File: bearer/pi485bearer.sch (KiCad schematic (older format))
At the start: 19 parts, among them P1 PWR, P2 Rasperry Pi, P3 Latch Disable, P4 TERM, Q1 2N4401, Q2 2N4401, Q3 2N4401, U1 NE555

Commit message: Renamed bearer.
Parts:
- C1: symbol CAP -> C
- D3: symbol DIODE -> D
- R7: value R -> 120
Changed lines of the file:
@@
 LIBS:contrib
 LIBS:valves
-LIBS:pi485carrier-cache
+LIBS:pi485bearer-cache
 EELAYER 26 0
 EELAYER END
@@
 encoding utf-8
 Sheet 1 2
-Title "Pi485"
+Title "Pi485 Bearer"
 Date "2017-01-18"
 Rev "1.1.0"
 Comp "Bryan Varner"
 Comment1 ""
-Comment2 "Size resistor values R1, R3, and R7 appropriately for your LED choices."
+Comment2 "Size resistor values R3 and R4 appropriately for your LED choices."
 Comment3 "Implements half-duplex with TX latched RE/DE"
 Comment4 "Raspberry Pi / Arduino UART to RS485"
@@
 $EndComp
 $Comp
-L CAP C1
+L C C1
 U 1 1 5881B0E4
 P 6150 5450
@@
 $EndComp
 $Comp
-L DIODE D3
+L D D3
 U 1 1 5881B0FC
 P 5850 4400
@@
 P 7550 3150
 F 0 "R7" H 7620 3196 50  0000 L CNN
-F 1 "R" H 7620 3105 50  0000 L CNN
+F 1 "120" H 7620 3105 50  0000 L CNN
 F 2 "Resistors_THT:Resistor_Horizontal_RM10mm" V 7480 3150 50  0001 C CNN
 F 3 "" H 7550 3150 50  0000 C CNN
@@
 Connection ~ 6400 4850
 Wire Wire Line
-	5000 5450 5900 5450
+	5000 5450 6000 5450
 Wire Wire Line
 	5500 5250 5500 5650
@@
 	6400 3800 6400 4000
 Wire Wire Line
-	5650 4400 4850 4400
+	5700 4400 4850 4400
 Wire Wire Line
 	2900 4300 2900 4850
@@
 Connection ~ 4000 3000
 Wire Wire Line
-	6050 4400 6400 4400
+	6000 4400 6400 4400
 Connection ~ 6400 5050
 Wire Wire Line
@@
 	6650 4650 6650 3450
 Wire Wire Line
-	6650 3450 5800 3450
-Wire Wire Line
-	5800 3450 5800 2850
+	5800 3450 6650 3450
+Wire Wire Line
+	5800 2850 5800 3450
 Wire Wire Line
 	5800 3000 5900 3000
@@
 Wire Wire Line
 	5400 2000 7200 2000
+Wire Wire Line
+	6400 5450 6300 5450
 $EndSCHEMATC

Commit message: Updated with TERM / RO values in schemas and PCBs
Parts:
- P3: value Latch Disable -> RO
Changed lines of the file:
@@
 P 4800 5400
 F 0 "P3" H 4800 5550 50  0000 C CNN
-F 1 "Latch Disable" V 4900 5400 50  0000 C CNN
+F 1 "RO" V 4900 5400 50  0000 C CNN
 F 2 "Pin_Headers:Pin_Header_Straight_1x02" H 5450 5650 50  0001 C CNN
 F 3 "" H 4800 5400 50  0000 C CNN

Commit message: Low-side NPN switching. We'll see if things 'floating' causes issues... if so, I'll have to order a few PNP's to use for high-side switching.
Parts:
- Q1, Q2, Q3: symbol BC413 -> Q_NPN_EBC
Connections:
- net GND: now also Q3.1 (E); no longer C1.2, D1.1 (K), D2.1 (K), P3.1 (P1), Q1.3 (E), Q2.3 (E), U1.1 (GND)
- net VCC: now also R1.2, R2.2, R6.2, U1.4 (R), U1.8 (VCC); no longer Q3.1 (C)
- net at D1.2 (A), R1.1: now also Q1.3 (C); no longer Q1.1 (C)
- net at D2.2 (A), R2.1: now also Q2.3 (C); no longer Q2.1 (C)
- removed net lctec485/VCIN: Q3.3 (E), R1.2, R2.2, R6.2, U1.4 (R), U1.8 (VCC)
- new net lctec485/GND: C1.2, D1.1 (K), D2.1 (K), P3.1 (P1), Q1.1 (E), Q2.1 (E), Q3.3 (C), U1.1 (GND)
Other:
- moved on the sheet: C1, D1, D2, D3, P3, R1, R2, R3, R4, R5, R6, U1

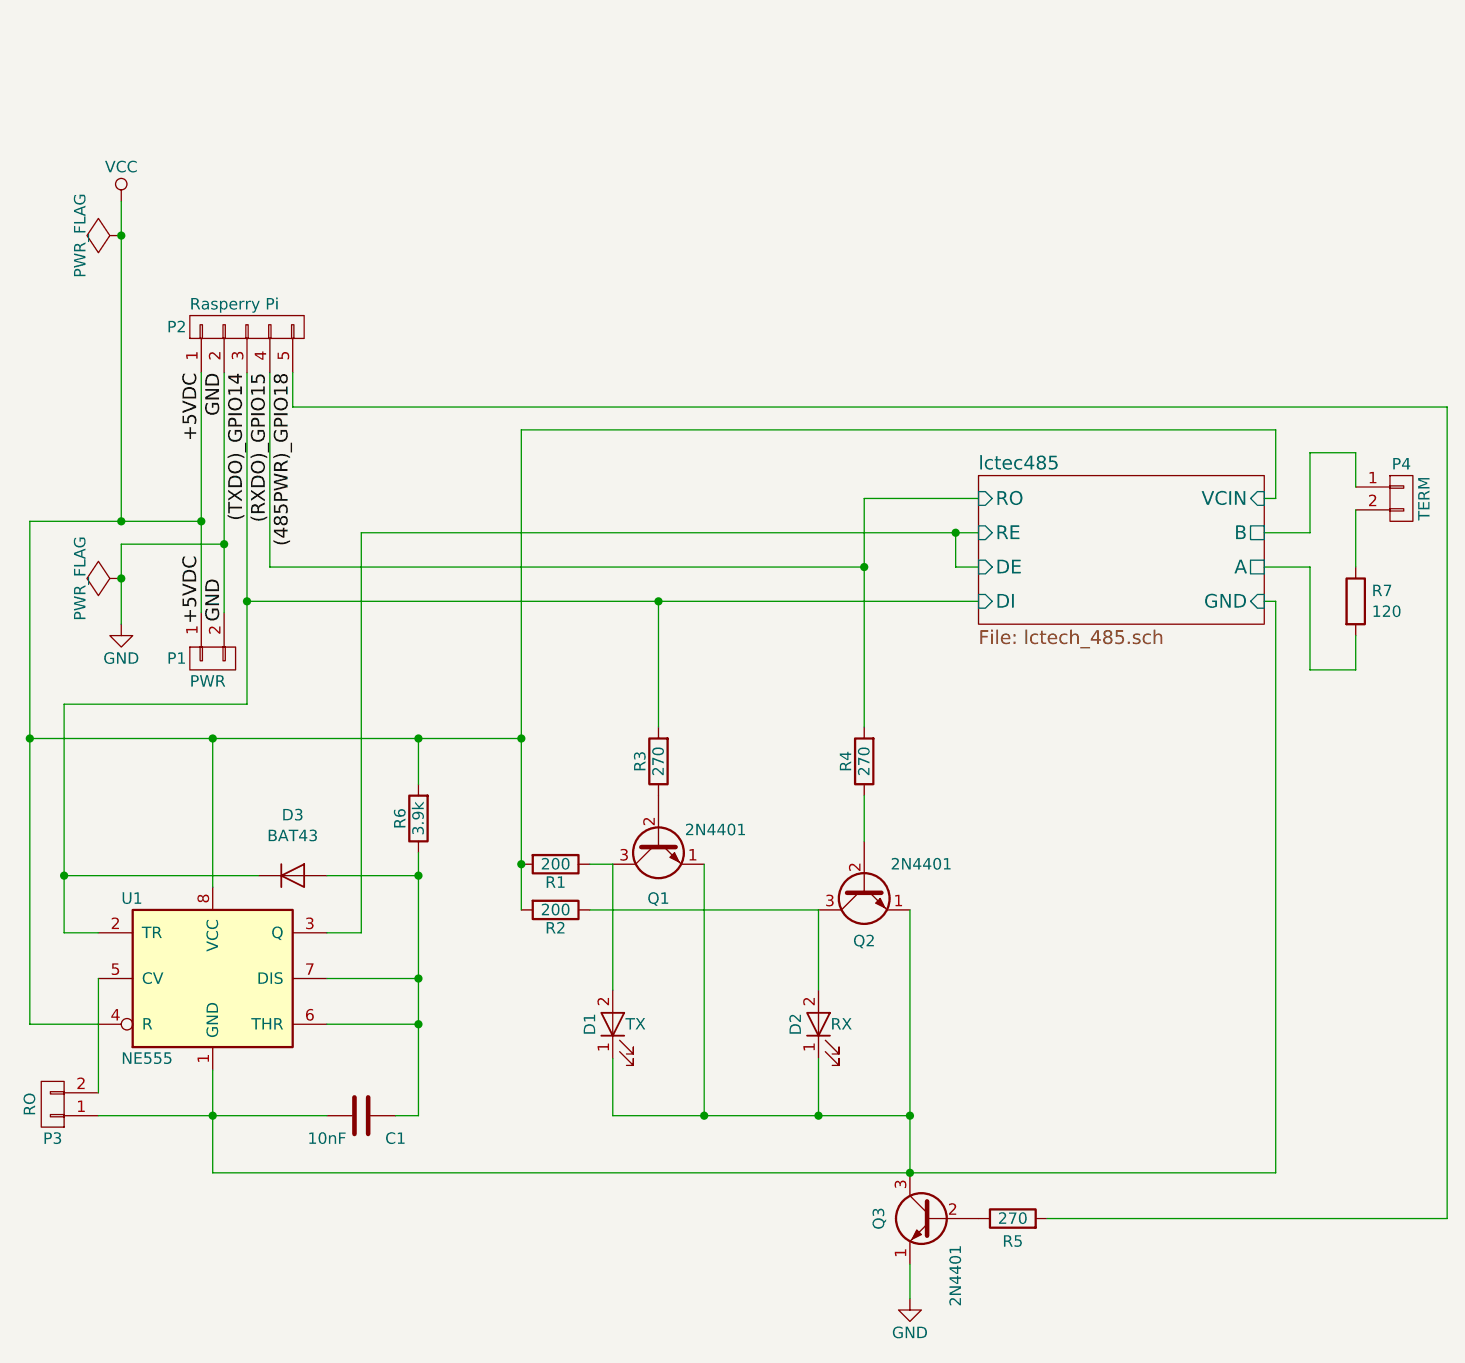
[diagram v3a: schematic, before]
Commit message: high-side PNP power switching for the bearer.
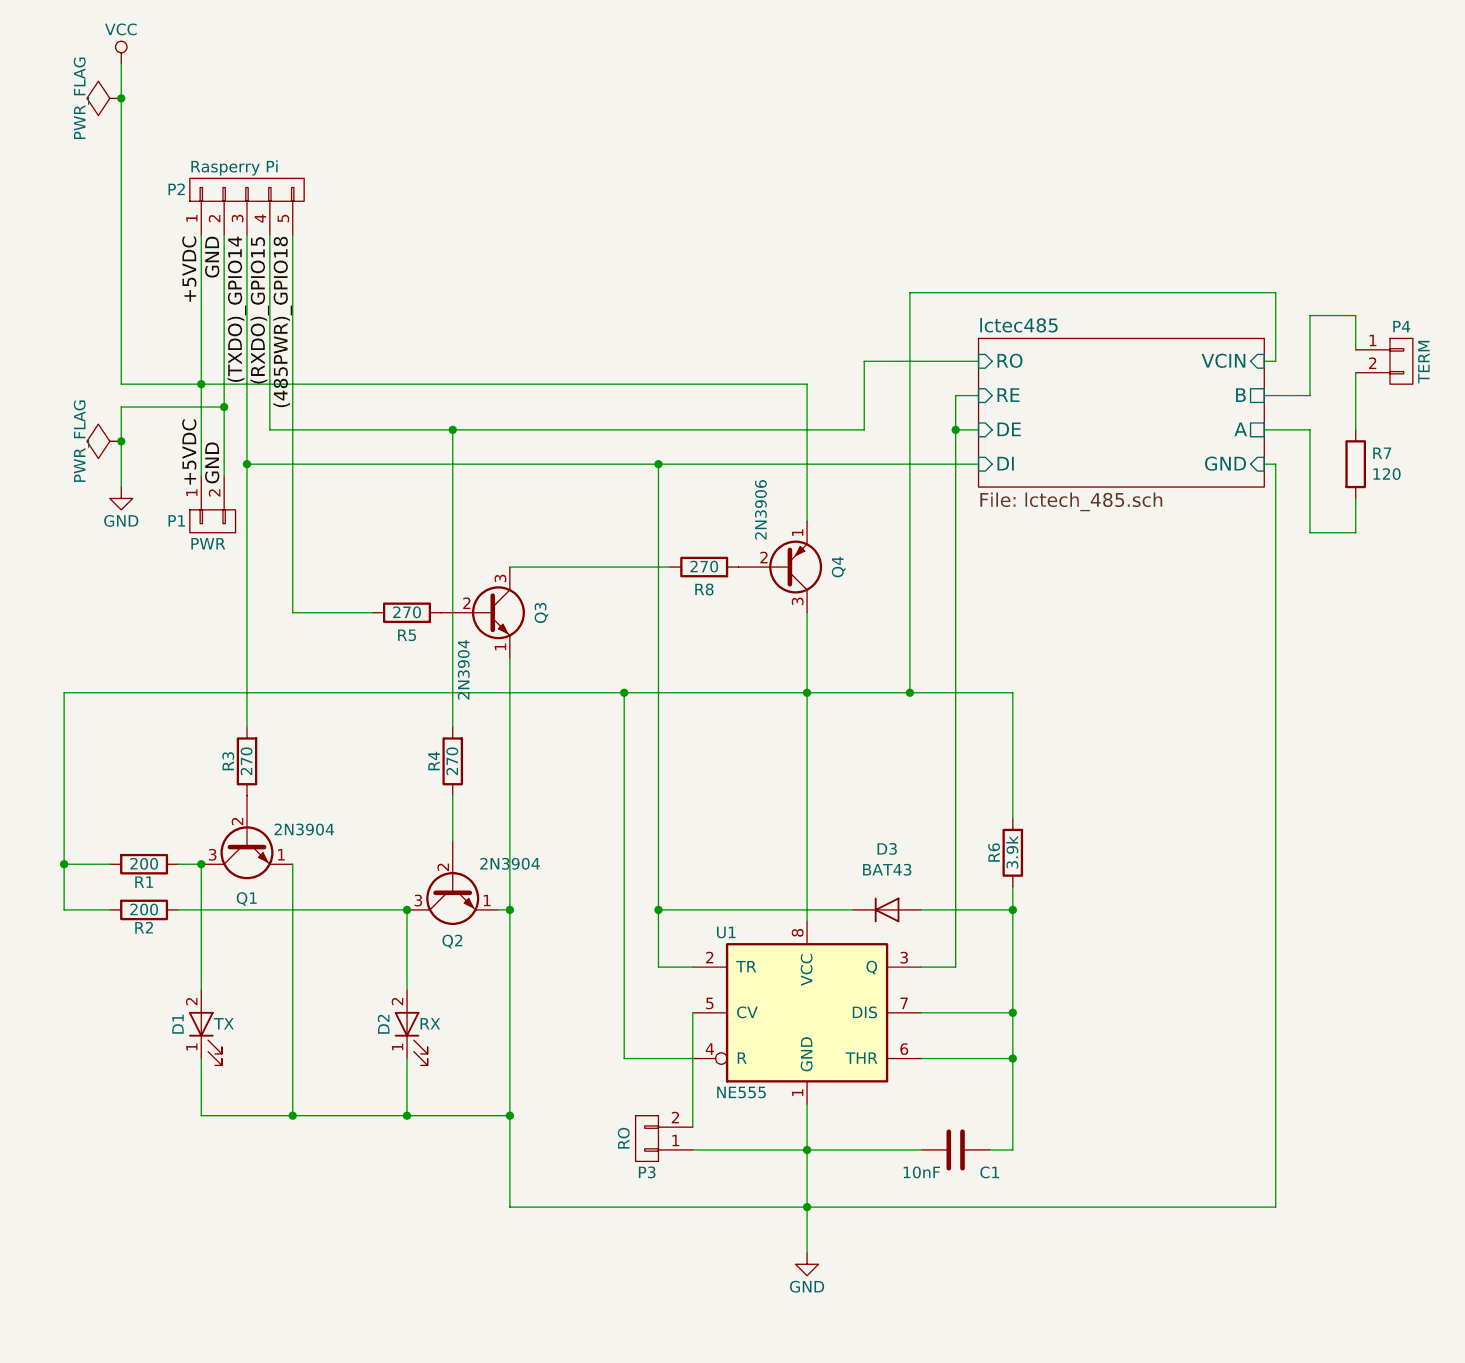
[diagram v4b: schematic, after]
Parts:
- added Q4: 2N3906, TO_SOT_Packages_THT:TO-92_Inline_Wide, symbol Q_PNP_EBC
- added R8: 270, Resistors_THT:Resistor_Horizontal_RM10mm, symbol R
- Q1, Q2, Q3: value 2N4401 -> 2N3904
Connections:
- net (485PWR)_GPIO18: now also R5.1; no longer R5.2
- net GND: now also C1.2, D1.1 (K), D2.1 (K), P3.1 (P1), Q1.1 (E), Q2.1 (E), U1.1 (GND)
- net VCC: now also Q4.1 (E); no longer R1.2, R2.2, R6.2, U1.4 (R), U1.8 (VCC)
- net at Q3.2 (B): now also R5.2; no longer R5.1
- removed net lctec485/GND: C1.2, D1.1 (K), D2.1 (K), P3.1 (P1), Q1.1 (E), Q2.1 (E), Q3.3 (C), U1.1 (GND)
- new net: Q3.3 (C), R8.1
- new net: Q4.2 (B), R8.2
- new net lctec485/VCIN: Q4.3 (C), R1.2, R2.2, R6.2, U1.4 (R), U1.8 (VCC)
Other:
- moved on the sheet: C1, D1, D2, D3, P1, P2, P3, P4, Q1, Q2, Q3, R1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

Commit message: 1.1.1 schematics, trace plots, etc.
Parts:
- added C2: 10nF, Capacitors_THT:C_Rect_L4_W2.5_P2.5, symbol C
- added R9: 4.7k, Resistors_THT:Resistor_Horizontal_RM15mm, symbol R
- C1: footprint Capacitors_THT:C_Rect_L7_W2.5_P5 -> Capacitors_THT:C_Rect_L4_W2.5_P2.5
- R1, R2, R4, R5, R8: footprint Resistors_THT:Resistor_Horizontal_RM10mm -> Resistors_THT:Resistor_Horizontal_RM7mm
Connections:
- net GND: now also P3.2 (P2), C2.1, R9.2; no longer P3.1 (P1)
- net lctec485/DE: now also R9.1
- net at U1.5 (CV): now also P3.1 (P1), C2.2; no longer P3.2 (P2)
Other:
- moved on the sheet: P3
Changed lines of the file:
@@
 Sheet 1 2
 Title "Pi485 Bearer"
-Date "2017-02-12"
-Rev "1.1.0"
+Date "2017-02-20"
+Rev "1.1.1"
 Comp "Bryan Varner"
 Comment1 ""
@@
 F 0 "C1" V 5900 5700 50  0000 C CNN
 F 1 "10nF" V 5900 5400 50  0000 C CNN
-F 2 "Capacitors_THT:C_Rect_L7_W2.5_P5" V 6000 5250 50  0001 C CNN
+F 2 "Capacitors_THT:C_Rect_L4_W2.5_P2.5" V 6000 5250 50  0001 C CNN
 F 3 "" H 5800 5550 50  0000 C CNN
 	1    5800 5550
@@
 F 0 "R2" V 2330 4500 50  0000 C CNN
 F 1 "200" V 2250 4500 50  0000 C CNN
-F 2 "Resistors_THT:Resistor_Horizontal_RM10mm" V 2400 3800 50  0001 C CNN
+F 2 "Resistors_THT:Resistor_Horizontal_RM7mm" V 2400 3800 50  0001 C CNN
 F 3 "" H 2250 4500 50  0000 C CNN
 	1    2250 4500
@@
 F 0 "R1" V 2330 4300 50  0000 C CNN
 F 1 "200" V 2250 4300 50  0000 C CNN
-F 2 "Resistors_THT:Resistor_Horizontal_RM10mm" V 2400 3600 50  0001 C CNN
+F 2 "Resistors_THT:Resistor_Horizontal_RM7mm" V 2400 3600 50  0001 C CNN
 F 3 "" H 2250 4300 50  0000 C CNN
 	1    2250 4300
@@
 F 0 "R4" V 3680 3850 50  0000 C CNN
 F 1 "270" V 3600 3850 50  0000 C CNN
-F 2 "Resistors_THT:Resistor_Horizontal_RM10mm" V 3750 3150 50  0001 C CNN
+F 2 "Resistors_THT:Resistor_Horizontal_RM7mm" V 3750 3150 50  0001 C CNN
 F 3 "" H 3600 3850 50  0000 C CNN
 	1    3600 3850
@@
 $EndComp
 $Comp
-L CONN_01X02 P3
-U 1 1 5881B0FD
-P 4450 5500
-F 0 "P3" H 4450 5650 50  0000 C CNN
-F 1 "RO" V 4550 5500 50  0000 C CNN
-F 2 "Pin_Headers:Pin_Header_Straight_1x02" H 5100 5750 50  0001 C CNN
-F 3 "" H 4450 5500 50  0000 C CNN
-	1    4450 5500
-	-1   0    0    1
-$EndComp
-$Comp
 L R R5
 U 1 1 5881B0FE
@@
 F 0 "R5" V 3300 3200 50  0000 C CNN
 F 1 "270" V 3400 3200 50  0000 C CNN
-F 2 "Resistors_THT:Resistor_Horizontal_RM10mm" V 3550 2500 50  0001 C CNN
+F 2 "Resistors_THT:Resistor_Horizontal_RM7mm" V 3550 2500 50  0001 C CNN
 F 3 "" H 3400 3200 50  0000 C CNN
 	1    3400 3200
@@
 Connection ~ 6050 4950
 Wire Wire Line
-	4650 5550 5650 5550
+	4400 5500 4550 5500
+Wire Wire Line
+	4550 5550 5650 5550
 Wire Wire Line
 	5150 5350 5150 6000
@@
 Connection ~ 6050 5150
 Wire Wire Line
-	4650 5450 4650 4950
+	4150 4950 4650 4950
 Wire Wire Line
 	2500 5400 3850 5400
@@
 	7150 2550 7200 2550
 Wire Wire Line
-	7200 5800 7200 2550
+	7200 2550 7200 5800
 Wire Wire Line
 	5400 2100 5900 2100
@@
 	5800 2250 5800 4750
 Wire Wire Line
-	5800 4750 5650 4750
-Wire Wire Line
-	3850 5800 7200 5800
+	5650 4750 6300 4750
+Wire Wire Line
+	7200 5800 3850 5800
 Wire Wire Line
 	7200 1800 7200 2100
@@
 F 0 "R8" V 4600 3000 50  0000 C CNN
 F 1 "270" V 4700 3000 50  0000 C CNN
-F 2 "Resistors_THT:Resistor_Horizontal_RM10mm" V 4850 2300 50  0001 C CNN
+F 2 "Resistors_THT:Resistor_Horizontal_RM7mm" V 4850 2300 50  0001 C CNN
 F 3 "" H 4700 3000 50  0000 C CNN
 	1    4700 3000
@@
 Connection ~ 4350 3550
 Connection ~ 4500 2550
+$Comp
+L R R9
+U 1 1 58A868D1
+P 6300 5000
+F 0 "R9" V 6380 5000 50  0000 C CNN
+F 1 "4.7k" V 6300 5000 50  0000 C CNN
+F 2 "Resistors_THT:Resistor_Horizontal_RM15mm" H 5400 5000 50  0001 C CNN
+F 3 "" H 6300 5000 50  0000 C CNN
+	1    6300 5000
+	1    0    0    -1
+$EndComp
+Connection ~ 5800 4750
+Wire Wire Line
+	6300 5150 6300 5800
+Connection ~ 6300 5800
+$Comp
+L C C2
+U 1 1 58A86CE6
+P 4350 5650
+F 0 "C2" V 4450 5800 50  0000 C CNN
+F 1 "10nF" V 4450 5500 50  0000 C CNN
+F 2 "Capacitors_THT:C_Rect_L4_W2.5_P2.5" V 4550 5350 50  0001 C CNN
+F 3 "" H 4350 5650 50  0000 C CNN
+	1    4350 5650
+	0    1    1    0
+$EndComp
+Wire Wire Line
+	4150 4950 4150 5650
+Wire Wire Line
+	6300 4750 6300 4850
+Wire Wire Line
+	4150 5650 4200 5650
+Wire Wire Line
+	4500 5650 4550 5650
+Wire Wire Line
+	4550 5650 4550 5500
+Connection ~ 4550 5550
+$Comp
+L CONN_01X02 P3
+U 1 1 5881B0FD
+P 4350 5300
+F 0 "P3" H 4350 5450 50  0000 C CNN
+F 1 "RO" V 4450 5300 50  0000 C CNN
+F 2 "Pin_Headers:Pin_Header_Straight_1x02" H 5000 5550 50  0001 C CNN
+F 3 "" H 4350 5300 50  0000 C CNN
+	1    4350 5300
+	0    -1   -1   0
+$EndComp
+Wire Wire Line
+	4300 5500 4150 5500
+Connection ~ 4150 5500
 $EndSCHEMATC

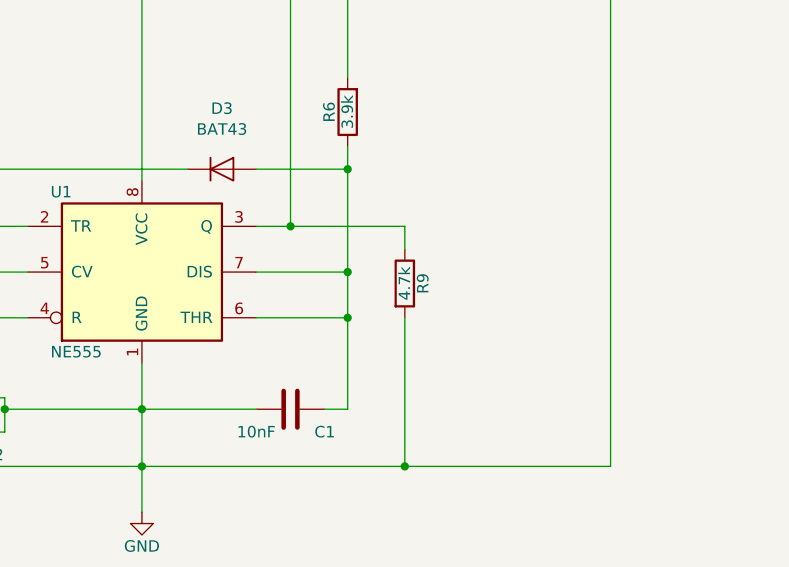
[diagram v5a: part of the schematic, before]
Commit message: Updates for jumpered biasing on standalone boards. The silly bearer modules you can just unsolder the biasing resistors if it becomes an issue. I should probably add jumpering for that too, but at this point, I just don't much care. A slight modification to those silly SMT boards really isn't that hard...
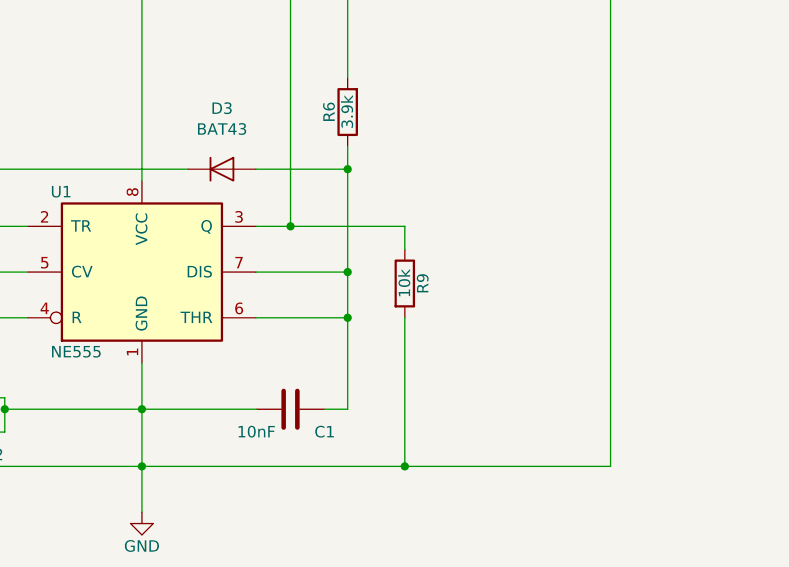
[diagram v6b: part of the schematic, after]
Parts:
- R9: value 4.7k -> 10k
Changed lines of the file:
@@
 P 6300 5000
 F 0 "R9" V 6380 5000 50  0000 C CNN
-F 1 "4.7k" V 6300 5000 50  0000 C CNN
+F 1 "10k" V 6300 5000 50  0000 C CNN
 F 2 "Resistors_THT:Resistor_Horizontal_RM15mm" H 5400 5000 50  0001 C CNN
 F 3 "" H 6300 5000 50  0000 C CNN
